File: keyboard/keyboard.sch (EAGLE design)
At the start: 33 parts, among them SW1 CHERRY_MX, SW10 CHERRY_MX, SW11 CHERRY_MX, SW12 CHERRY_MX, SW13 CHERRY_MX, SW14 CHERRY_MX, SW15 CHERRY_MX, SW16 CHERRY_MX, SW17 CHERRY_MX, SW18 CHERRY_MX, SW19 CHERRY_MX, SW2 CHERRY_MX, SW20 CHERRY_MX, SW21 CHERRY_MX, SW22 CHERRY_MX, SW23 CHERRY_MX, SW24 CHERRY_MX, SW25 CHERRY_MX, SW26 CHERRY_MX, SW27 CHERRY_MX, SW28 CHERRY_MX, SW3 CHERRY_MX, SW4 CHERRY_MX, SW5 CHERRY_MX, SW6 CHERRY_MX, SW7 CHERRY_MX, SW8 CHERRY_MX, SW9 CHERRY_MX

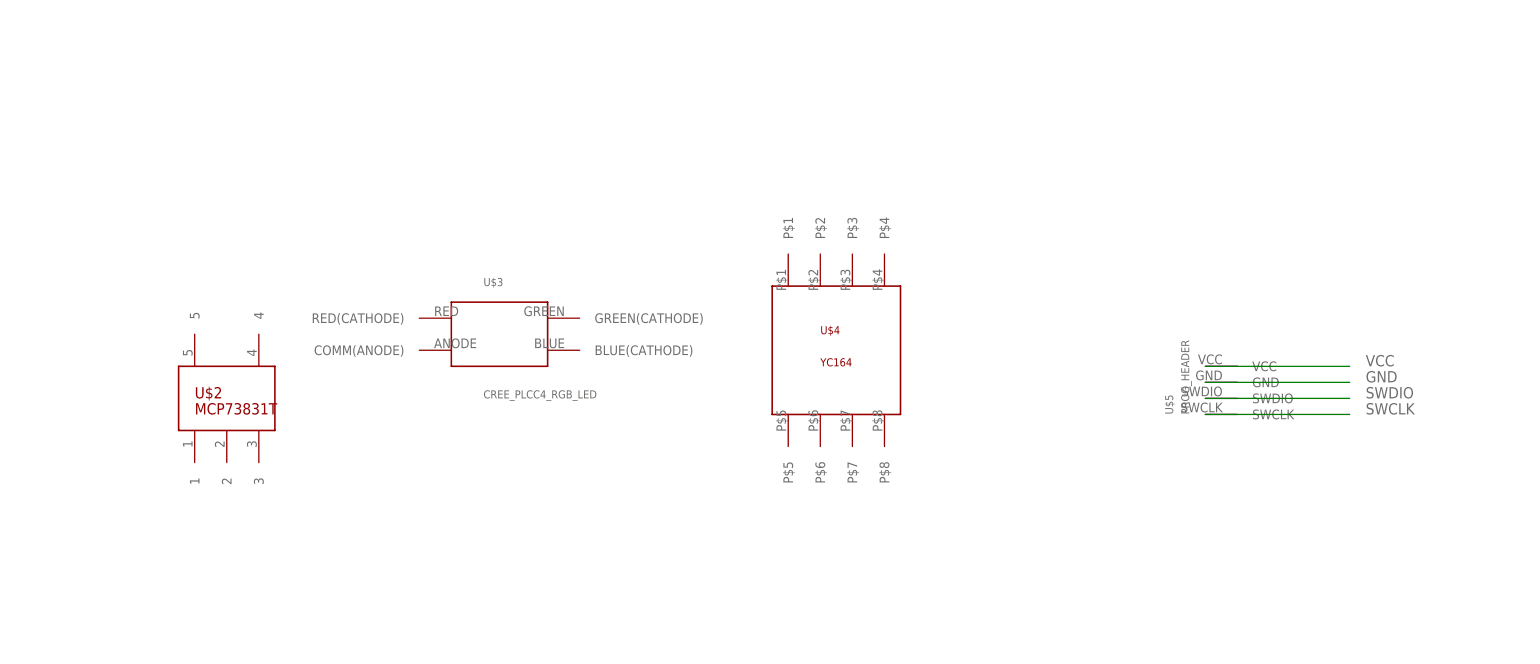
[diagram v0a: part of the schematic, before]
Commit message: connect mcp73831t charging circuit
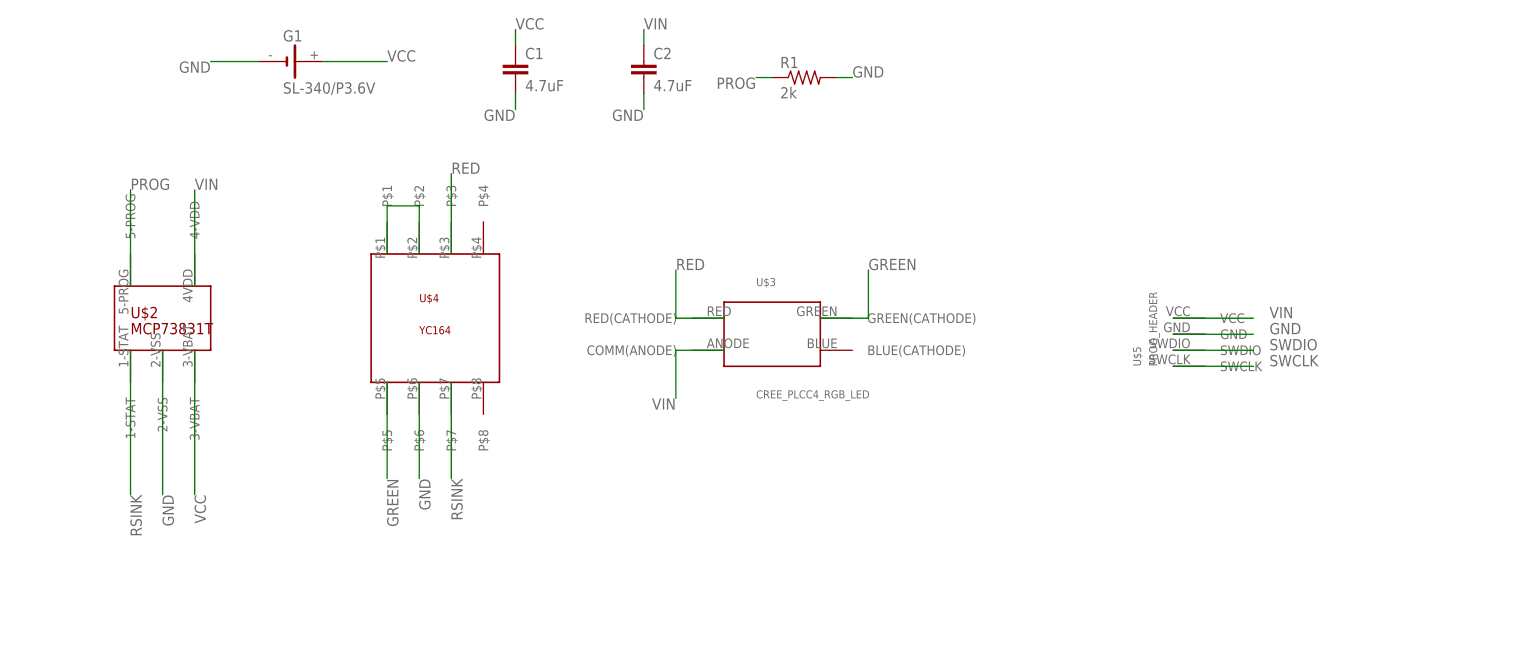
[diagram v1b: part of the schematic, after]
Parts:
- added C1, C2: 4.7uF, capacitor-wima:C2.5/5
- added G1: SL-340/P3.6V, battery:SL-340/P3.6V
- added R1: 2k, resistor:R-US_M1206
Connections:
- new net GREEN: U$3.GREEN(CATHODE), U$4.P$5
- new net N$3: U$4.P$1, U$4.P$2
- new net PROG: R1.1, U$2.5-PROG
- new net RED: U$3.RED(CATHODE), U$4.P$3
- new net RSINK: U$2.1-STAT, U$4.P$7
- new net VIN: C2.1, U$2.4-VDD, U$3.COMM(ANODE), U$5.VCC
- net GND: now also C1.2, C2.2, G1.-, R1.2, U$2.2-VSS, U$4.P$6
- net VCC: now also C1.1, G1.+, U$2.3-VBAT; no longer U$5.VCC
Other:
- moved on the sheet: U$2, U$3, U$4, U$5
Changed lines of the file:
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@@
 <part name="SW28" library="cherry_mx" deviceset="CHERRY_MX" device=""/>
 <part name="U$2" library="mcp73831t" deviceset="MCP73831T" device=""/>
+<part name="G1" library="battery" library_urn="urn:adsk.eagle:library:109" deviceset="SL-340/P3.6V" device="" package3d_urn="urn:adsk.eagle:package:4605/1"/>
+<part name="C1" library="capacitor-wima" library_urn="urn:adsk.eagle:library:116" deviceset="C" device="2.5/5" package3d_urn="urn:adsk.eagle:package:5407/1" value="4.7uF"/>
+<part name="C2" library="capacitor-wima" library_urn="urn:adsk.eagle:library:116" deviceset="C" device="2.5/5" package3d_urn="urn:adsk.eagle:package:5407/1" value="4.7uF"/>
+<part name="R1" library="resistor" library_urn="urn:adsk.eagle:library:348" deviceset="R-US_" device="M1206" package3d_urn="urn:adsk.eagle:package:26088/1" value="2k"/>
 </parts>
 <sheets>
@@
 <instances>
 <instance part="U$1" gate="G$1" x="124.46" y="-241.3"/>
-<instance part="U$3" gate="G$1" x="99.06" y="30.48"/>
-<instance part="U$4" gate="G$1" x="152.4" y="27.94"/>
-<instance part="U$5" gate="G$1" x="210.82" y="25.4"/>
+<instance part="U$3" gate="G$1" x="142.24" y="30.48"/>
+<instance part="U$4" gate="G$1" x="88.9" y="33.02"/>
+<instance part="U$5" gate="G$1" x="205.74" y="33.02"/>
 <instance part="SW1" gate="G$1" x="30.48" y="-35.56"/>
 <instance part="SW2" gate="G$1" x="71.12" y="-35.56"/>
@@
 <instance part="SW27" gate="G$1" x="198.12" y="-187.96"/>
 <instance part="SW28" gate="G$1" x="243.84" y="-205.74"/>
-<instance part="U$2" gate="G$1" x="55.88" y="20.32"/>
+<instance part="U$2" gate="G$1" x="45.72" y="33.02"/>
+<instance part="G1" gate="G$1" x="66.04" y="73.66"/>
+<instance part="C1" gate="G$1" x="101.6" y="73.66"/>
+<instance part="C2" gate="G$1" x="121.92" y="73.66"/>
+<instance part="R1" gate="G$1" x="147.32" y="71.12"/>
 </instances>
 <busses>
@@
 <segment>
 <pinref part="U$5" gate="G$1" pin="GND"/>
-<wire x1="210.82" y1="22.86" x2="233.68" y2="22.86" width="0.1524" layer="91"/>
-<label x="236.22" y="22.86" size="1.778" layer="95"/>
+<wire x1="205.74" y1="30.48" x2="218.44" y2="30.48" width="0.1524" layer="91"/>
+<label x="220.98" y="30.48" size="1.778" layer="95"/>
+</segment>
+<segment>
+<pinref part="U$2" gate="G$1" pin="2-VSS"/>
+<wire x1="45.72" y1="27.94" x2="45.72" y2="5.08" width="0.1524" layer="91"/>
+<label x="45.72" y="5.08" size="1.778" layer="95" rot="R270"/>
+</segment>
+<segment>
+<pinref part="U$4" gate="G$1" pin="P$6"/>
+<wire x1="86.36" y1="22.86" x2="86.36" y2="7.62" width="0.1524" layer="91"/>
+<label x="86.36" y="7.62" size="1.778" layer="95" rot="R270"/>
+</segment>
+<segment>
+<pinref part="G1" gate="G$1" pin="-"/>
+<wire x1="60.96" y1="73.66" x2="53.34" y2="73.66" width="0.1524" layer="91"/>
+<label x="53.34" y="73.66" size="1.778" layer="95" rot="R180"/>
+</segment>
+<segment>
+<pinref part="C1" gate="G$1" pin="2"/>
+<wire x1="101.6" y1="68.58" x2="101.6" y2="66.04" width="0.1524" layer="91"/>
+<label x="101.6" y="66.04" size="1.778" layer="95" rot="R180"/>
+</segment>
+<segment>
+<pinref part="C2" gate="G$1" pin="2"/>
+<wire x1="121.92" y1="68.58" x2="121.92" y2="66.04" width="0.1524" layer="91"/>
+<label x="121.92" y="66.04" size="1.778" layer="95" rot="R180"/>
+</segment>
+<segment>
+<pinref part="R1" gate="G$1" pin="2"/>
+<wire x1="152.4" y1="71.12" x2="154.94" y2="71.12" width="0.1524" layer="91"/>
+<label x="154.94" y="71.12" size="1.778" layer="95"/>
 </segment>
 </net>
@@
 <segment>
 <pinref part="U$5" gate="G$1" pin="SWDIO"/>
-<wire x1="210.82" y1="20.32" x2="233.68" y2="20.32" width="0.1524" layer="91"/>
-<label x="236.22" y="20.32" size="1.778" layer="95"/>
+<wire x1="205.74" y1="27.94" x2="218.44" y2="27.94" width="0.1524" layer="91"/>
+<label x="220.98" y="27.94" size="1.778" layer="95"/>
 </segment>
 </net>
@@
 <segment>
 <pinref part="U$5" gate="G$1" pin="SWCLK"/>
-<wire x1="210.82" y1="17.78" x2="233.68" y2="17.78" width="0.1524" layer="91"/>
-<label x="236.22" y="17.78" size="1.778" layer="95"/>
+<wire x1="205.74" y1="25.4" x2="218.44" y2="25.4" width="0.1524" layer="91"/>
+<label x="220.98" y="25.4" size="1.778" layer="95"/>
 </segment>
 </net>
@@
 </segment>
 <segment>
+<pinref part="U$2" gate="G$1" pin="3-VBAT"/>
+<wire x1="50.8" y1="27.94" x2="50.8" y2="5.08" width="0.1524" layer="91"/>
+<label x="50.8" y="5.08" size="1.778" layer="95" rot="R270"/>
+</segment>
+<segment>
+<pinref part="G1" gate="G$1" pin="+"/>
+<wire x1="71.12" y1="73.66" x2="81.28" y2="73.66" width="0.1524" layer="91"/>
+<label x="81.28" y="73.66" size="1.778" layer="95"/>
+</segment>
+<segment>
+<pinref part="C1" gate="G$1" pin="1"/>
+<wire x1="101.6" y1="76.2" x2="101.6" y2="78.74" width="0.1524" layer="91"/>
+<label x="101.6" y="78.74" size="1.778" layer="95"/>
+</segment>
+</net>
+<net name="RED" class="0">
+<segment>
+<pinref part="U$4" gate="G$1" pin="P$3"/>
+<wire x1="91.44" y1="43.18" x2="91.44" y2="55.88" width="0.1524" layer="91"/>
+<label x="91.44" y="55.88" size="1.778" layer="95"/>
+</segment>
+<segment>
+<pinref part="U$3" gate="G$1" pin="RED(CATHODE)"/>
+<wire x1="134.62" y1="33.02" x2="127" y2="33.02" width="0.1524" layer="91"/>
+<wire x1="127" y1="33.02" x2="127" y2="40.64" width="0.1524" layer="91"/>
+<label x="127" y="40.64" size="1.778" layer="95"/>
+</segment>
+</net>
+<net name="GREEN" class="0">
+<segment>
+<pinref part="U$3" gate="G$1" pin="GREEN(CATHODE)"/>
+<wire x1="149.86" y1="33.02" x2="157.48" y2="33.02" width="0.1524" layer="91"/>
+<wire x1="157.48" y1="33.02" x2="157.48" y2="40.64" width="0.1524" layer="91"/>
+<label x="157.48" y="40.64" size="1.778" layer="95"/>
+</segment>
+<segment>
+<pinref part="U$4" gate="G$1" pin="P$5"/>
+<wire x1="81.28" y1="22.86" x2="81.28" y2="7.62" width="0.1524" layer="91"/>
+<label x="81.28" y="7.62" size="1.778" layer="95" rot="R270"/>
+</segment>
+</net>
+<net name="N$3" class="0">
+<segment>
+<pinref part="U$4" gate="G$1" pin="P$1"/>
+<wire x1="81.28" y1="43.18" x2="81.28" y2="50.8" width="0.1524" layer="91"/>
+<pinref part="U$4" gate="G$1" pin="P$2"/>
+<wire x1="81.28" y1="50.8" x2="86.36" y2="50.8" width="0.1524" layer="91"/>
+<wire x1="86.36" y1="50.8" x2="86.36" y2="43.18" width="0.1524" layer="91"/>
+</segment>
+</net>
+<net name="RSINK" class="0">
+<segment>
+<pinref part="U$2" gate="G$1" pin="1-STAT"/>
+<wire x1="40.64" y1="27.94" x2="40.64" y2="5.08" width="0.1524" layer="91"/>
+<label x="40.64" y="5.08" size="1.778" layer="95" rot="R270"/>
+</segment>
+<segment>
+<pinref part="U$4" gate="G$1" pin="P$7"/>
+<wire x1="91.44" y1="22.86" x2="91.44" y2="7.62" width="0.1524" layer="91"/>
+<label x="91.44" y="7.62" size="1.778" layer="95" rot="R270"/>
+</segment>
+</net>
+<net name="VIN" class="0">
+<segment>
 <pinref part="U$5" gate="G$1" pin="VCC"/>
-<wire x1="210.82" y1="25.4" x2="233.68" y2="25.4" width="0.1524" layer="91"/>
-<label x="236.22" y="25.4" size="1.778" layer="95"/>
+<wire x1="205.74" y1="33.02" x2="218.44" y2="33.02" width="0.1524" layer="91"/>
+<label x="220.98" y="33.02" size="1.778" layer="95"/>
+</segment>
+<segment>
+<pinref part="U$3" gate="G$1" pin="COMM(ANODE)"/>
+<wire x1="134.62" y1="27.94" x2="127" y2="27.94" width="0.1524" layer="91"/>
+<wire x1="127" y1="27.94" x2="127" y2="20.32" width="0.1524" layer="91"/>
+<label x="127" y="20.32" size="1.778" layer="95" rot="R180"/>
+</segment>
+<segment>
+<pinref part="C2" gate="G$1" pin="1"/>
+<wire x1="121.92" y1="76.2" x2="121.92" y2="78.74" width="0.1524" layer="91"/>
+<label x="121.92" y="78.74" size="1.778" layer="95"/>
+</segment>
+<segment>
+<pinref part="U$2" gate="G$1" pin="4-VDD"/>
+<wire x1="50.8" y1="38.1" x2="50.8" y2="53.34" width="0.1524" layer="91"/>
+<label x="50.8" y="53.34" size="1.778" layer="95"/>
+</segment>
+</net>
+<net name="PROG" class="0">
+<segment>
+<pinref part="R1" gate="G$1" pin="1"/>
+<wire x1="142.24" y1="71.12" x2="139.7" y2="71.12" width="0.1524" layer="91"/>
+<label x="139.7" y="71.12" size="1.778" layer="95" rot="R180"/>
+</segment>
+<segment>
+<pinref part="U$2" gate="G$1" pin="5-PROG"/>
+<wire x1="40.64" y1="38.1" x2="40.64" y2="53.34" width="0.1524" layer="91"/>
+<label x="40.64" y="53.34" size="1.778" layer="95"/>
 </segment>
 </net>
@@
 </schematic>
 </drawing>
+<compatibility>
+<note version="8.2" severity="warning">
+Since Version 8.2, EAGLE supports online libraries. The ids
+of those online libraries will not be understood (or retained)
+with this version.
+</note>
+<note version="8.3" severity="warning">
+Since Version 8.3, EAGLE supports URNs for individual library
+assets (packages, symbols, and devices). The URNs of those assets
+will not be understood (or retained) with this version.
+</note>
+<note version="8.3" severity="warning">
+Since Version 8.3, EAGLE supports the association of 3D packages
+with devices in libraries, schematics, and board files. Those 3D
+packages will not be understood (or retained) with this version.
+</note>
+</compatibility>
 </eagle>

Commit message: update resistors
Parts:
- removed R1: 2k, resistor:R-US_M1206
- removed U$4: YC164, yc164:YC164
- added R2, R3, R4: (no value), resistor:R-US_R1210
- added U$6: CORE51822B, core51822b:CORE51822B
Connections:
- removed net N$3: U$4.P$1, U$4.P$2
- net GND: now also R2.2, R3.2, U$6.GND0, U$6.GND1; no longer R1.2, U$4.P$6
- net GREEN: now also R3.1; no longer U$4.P$5
- net PROG: now also R2.1; no longer R1.1
- net RED: now also R4.1; no longer U$4.P$3
- net RSINK: now also R4.2; no longer U$4.P$7
- net SW1: now also U$6.P24
- net SW10: now also U$6.P13
- net SW11: now also U$6.P28
- net SW12: now also U$6.P02
- net SW13: now also U$6.P06
- net SW14: now also U$6.P10
- net SW15: now also U$6.P14
- net SW16: now also U$6.P29
- net SW17: now also U$6.P03
- net SW18: now also U$6.P07
- net SW19: now also U$6.P11
- net SW2: now also U$6.P00
- net SW20: now also U$6.P15
- net SW21: now also U$6.P16
- net SW22: now also U$6.P17
- net SW23: now also U$6.P23
- net SW24: now also U$6.P22
- net SW25: now also U$6.P18
- net SW26: now also U$6.P19
- net SW27: now also U$6.P20
- net SW28: now also U$6.P21
- net SW3: now also U$6.P04
- net SW4: now also U$6.P08
- net SW5: now also U$6.P12
- net SW6: now also U$6.P25
- net SW7: now also U$6.P01
- net SW8: now also U$6.P05
- net SW9: now also U$6.P09
- net SWCLK: now also U$6.SWCLK
- net SWDIO: now also U$6.SWDIO
- net VCC: now also U$6.VCC
